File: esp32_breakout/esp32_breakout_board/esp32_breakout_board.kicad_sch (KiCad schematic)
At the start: 7 parts, among them U4 ESP32-S3-MINI-1

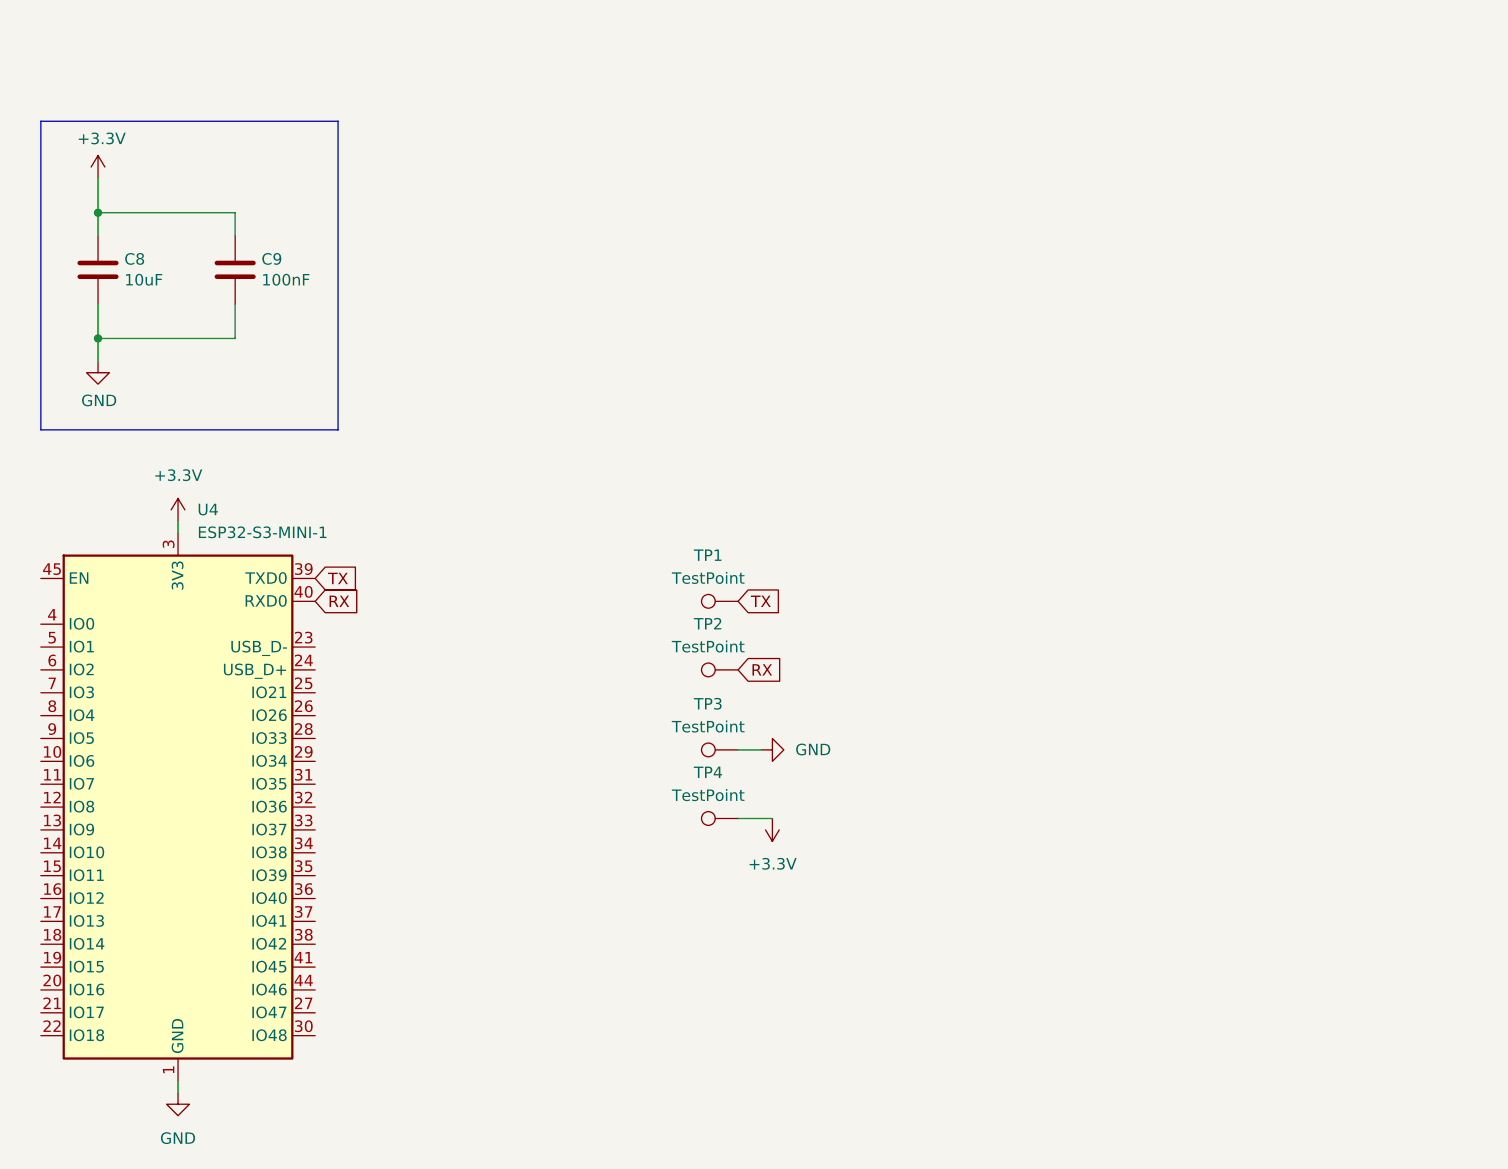
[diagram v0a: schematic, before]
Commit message: Included resistors for EN/GPIO0 on ESP32
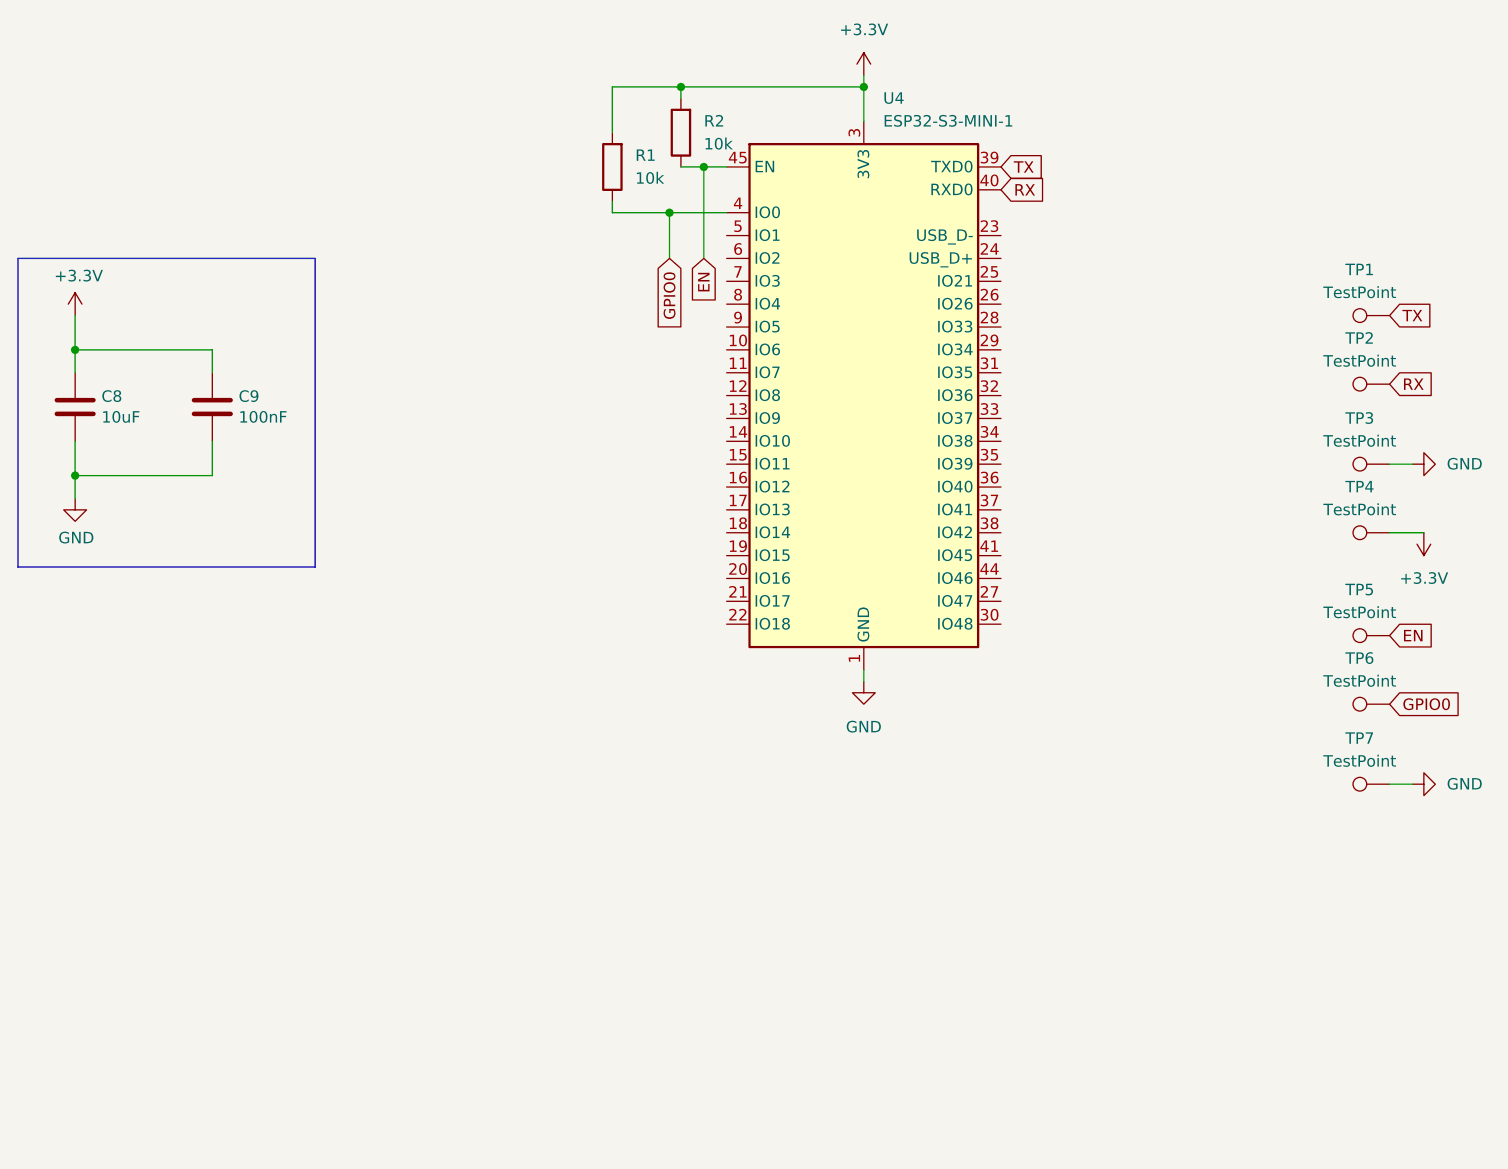
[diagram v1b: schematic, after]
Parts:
- added R1, R2: 10k, RC0402FR-7D4K7L:RESC1005X40N, symbol ScottoKeebs:Placeholder_Resistor
- added TP5, TP6, TP7: TestPoint, TestPoint:TestPoint_THTPad_D2.0mm_Drill1.0mm, symbol Connector:TestPoint
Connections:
- net +3.3V: now also R1.2, R2.2
- net GND: now also TP7.1
- net GPIO0: now reaches U4.4 (IO0)
- net GPIO0: now also R1.1, TP6.1
- net EN: now reaches U4.45 (EN)
- net EN: now also R2.1, TP5.1
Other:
- moved on the sheet: C8, C9, TP1, TP2, TP3, TP4, U4
